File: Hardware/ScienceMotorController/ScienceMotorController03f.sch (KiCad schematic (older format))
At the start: 18 parts

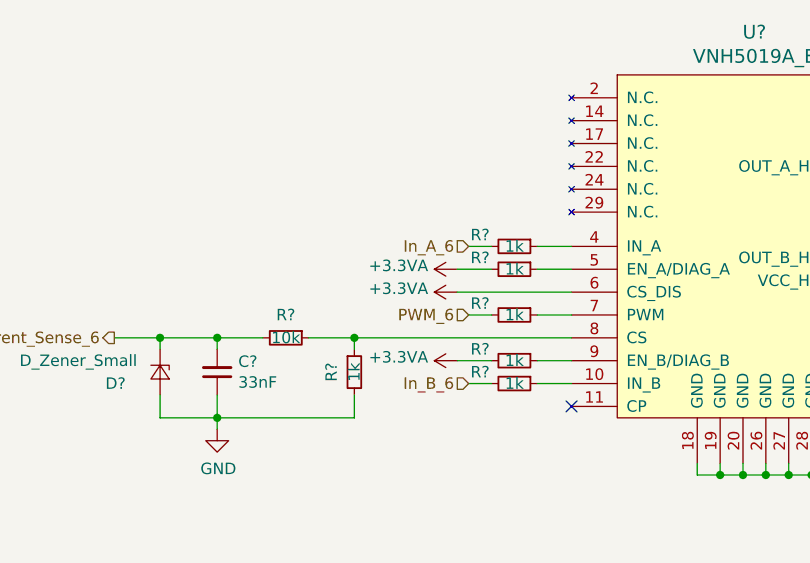
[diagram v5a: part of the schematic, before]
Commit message: Fixed 3.3V, added encoders
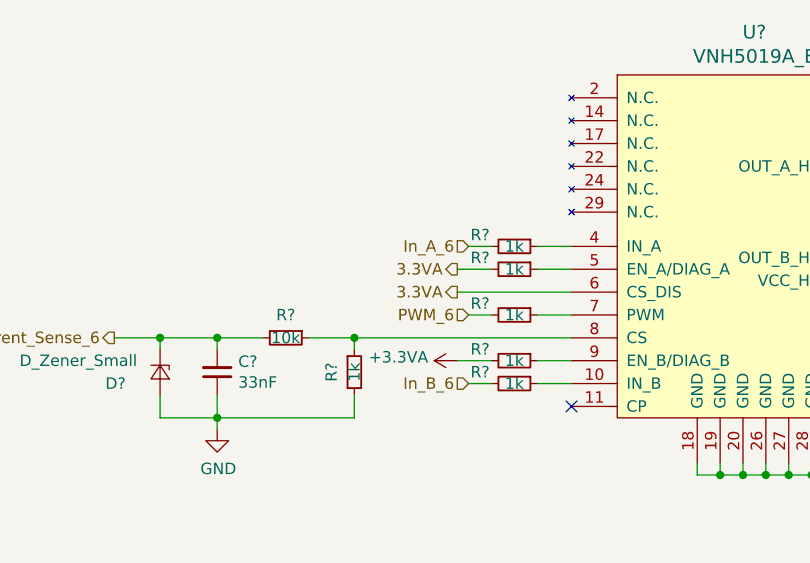
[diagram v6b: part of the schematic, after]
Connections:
- net +3.3VA: no longer R?.2, U?.6 (CS_DIS)
- new net 3.3VA: R?.2, U?.6 (CS_DIS)
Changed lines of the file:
@@
 $Descr A4 11693 8268
 encoding utf-8
-Sheet 8 10
+Sheet 8 11
 Title ""
 Date ""
@@
 $Comp
 L power:+3.3VA #PWR?
-U 1 1 5F83FF6A
-P 5150 3750
-AR Path="/5F7D111E/5FA66A7C/5F83FF6A" Ref="#PWR?"  Part="1"
-AR Path="/5F908300/5F83FF6A" Ref="#PWR?"  Part="1"
-AR Path="/5F7148FA/5FA34ADD/5F83FF6A" Ref="#PWR?"  Part="1"
-F 0 "#PWR?" H 5150 3600 50  0001 C CNN
-F 1 "+3.3VA" V 5165 3877 50  0000 L CNN
-F 2 "" H 5150 3750 50  0001 C CNN
-F 3 "" H 5150 3750 50  0001 C CNN
-	1    5150 3750
-	0    -1   -1   0
-$EndComp
-$Comp
-L power:+3.3VA #PWR?
-U 1 1 5F8408BA
-P 5150 3850
-AR Path="/5F7D111E/5FA66A7C/5F8408BA" Ref="#PWR?"  Part="1"
-AR Path="/5F908300/5F8408BA" Ref="#PWR?"  Part="1"
-AR Path="/5F7148FA/5FA34ADD/5F8408BA" Ref="#PWR?"  Part="1"
-F 0 "#PWR?" H 5150 3700 50  0001 C CNN
-F 1 "+3.3VA" V 5165 3977 50  0000 L CNN
-F 2 "" H 5150 3850 50  0001 C CNN
-F 3 "" H 5150 3850 50  0001 C CNN
-	1    5150 3850
-	0    -1   -1   0
-$EndComp
-$Comp
-L power:+3.3VA #PWR?
 U 1 1 5F840B1F
 P 5150 4150
@@
 Text HLabel 3650 4050 0    50   Output ~ 0
 Current_Sense_6
+Text HLabel 5150 3750 0    50   Output ~ 0
+3.3VA
+Text HLabel 5150 3850 0    50   Output ~ 0
+3.3VA
 $EndSCHEMATC

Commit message: added logic line
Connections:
- net 3.3VA is gone; now on net 3.3V: R?.2, U?.6 (CS_DIS)
- net +3.3VA renamed 3.3V
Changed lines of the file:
@@
-$EndComp
-$Comp
-L power:+3.3VA #PWR?
-U 1 1 5F840B1F
-P 5150 4150
-AR Path="/5F7D111E/5FA66A7C/5F840B1F" Ref="#PWR?"  Part="1"
-AR Path="/5F908300/5F840B1F" Ref="#PWR?"  Part="1"
-AR Path="/5F7148FA/5FA34ADD/5F840B1F" Ref="#PWR?"  Part="1"
-F 0 "#PWR?" H 5150 4000 50  0001 C CNN
-F 1 "+3.3VA" V 5165 4277 50  0000 L CNN
-F 2 "" H 5150 4150 50  0001 C CNN
-F 3 "" H 5150 4150 50  0001 C CNN
-	1    5150 4150
-	0    -1   -1   0
 $EndComp
 $Comp
@@
 Current_Sense_6
 Text HLabel 5150 3750 0    50   Output ~ 0
-3.3VA
+3.3V
 Text HLabel 5150 3850 0    50   Output ~ 0
-3.3VA
+3.3V
+Text HLabel 5150 4150 0    50   Output ~ 0
+3.3V
 $EndSCHEMATC

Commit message: annotated
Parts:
- C7: renamed from C?; footprint (none) -> Capacitor_SMD:C_0603_1608Metric_Pad1.05x0.95mm_HandSolder
- gave numbers to parts that had none: 16
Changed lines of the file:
@@
 AR Path="/5F7D111E/5FA66A7C/5FACB523" Ref="U?"  Part="1"
 AR Path="/5F908300/5FACB523" Ref="U?"  Part="1"
-AR Path="/5F7148FA/5FA34ADD/5FACB523" Ref="U?"  Part="1"
-F 0 "U?" H 6450 6087 60  0000 C CNN
+AR Path="/5F7148FA/5FA34ADD/5FACB523" Ref="U7"  Part="1"
+F 0 "U7" H 6450 6087 60  0000 C CNN
 F 1 "VNH5019A_E" H 6450 5981 60  0000 C CNN
 F 2 "" H 5850 5700 60  0001 C CNN
@@
 AR Path="/5F7D111E/5FA66A7C/5FACB540" Ref="R?"  Part="1"
 AR Path="/5F908300/5FACB540" Ref="R?"  Part="1"
-AR Path="/5F7148FA/5FA34ADD/5FACB540" Ref="R?"  Part="1"
-F 0 "R?" V 5350 3800 50  0000 C CNN
+AR Path="/5F7148FA/5FA34ADD/5FACB540" Ref="R46"  Part="1"
+F 0 "R46" V 5350 3800 50  0000 C CNN
 F 1 "1k" V 5400 3950 50  0000 C CNN
 F 2 "" H 5400 3950 50  0001 C CNN
@@
 AR Path="/5F7D111E/5FA66A7C/5FACB546" Ref="R?"  Part="1"
 AR Path="/5F908300/5FACB546" Ref="R?"  Part="1"
-AR Path="/5F7148FA/5FA34ADD/5FACB546" Ref="R?"  Part="1"
-F 0 "R?" V 4600 4200 50  0000 C CNN
+AR Path="/5F7148FA/5FA34ADD/5FACB546" Ref="R43"  Part="1"
+F 0 "R43" V 4600 4200 50  0000 C CNN
 F 1 "1k" V 4700 4200 50  0000 C CNN
 F 2 "" H 4700 4200 50  0001 C CNN
@@
 AR Path="/5F7D111E/5FA66A7C/5FACB54C" Ref="C?"  Part="1"
 AR Path="/5F908300/5FACB54C" Ref="C?"  Part="1"
-AR Path="/5F7148FA/5FA34ADD/5FACB54C" Ref="C?"  Part="1"
-F 0 "C?" H 4008 4154 50  0000 R CNN
+AR Path="/5F7148FA/5FA34ADD/5FACB54C" Ref="C7"  Part="1"
+F 0 "C7" H 4008 4154 50  0000 R CNN
 F 1 "33nF" H 4008 4245 50  0000 R CNN
-F 2 "" H 4100 4200 50  0001 C CNN
+F 2 "Capacitor_SMD:C_0603_1608Metric_Pad1.05x0.95mm_HandSolder" H 4100 4200 50  0001 C CNN
 F 3 "~" H 4100 4200 50  0001 C CNN
 	1    4100 4200
@@
 AR Path="/5F7D111E/5FA66A7C/5FACB552" Ref="D?"  Part="1"
 AR Path="/5F908300/5FACB552" Ref="D?"  Part="1"
-AR Path="/5F7148FA/5FA34ADD/5FACB552" Ref="D?"  Part="1"
-F 0 "D?" V 3900 4050 50  0000 R CNN
+AR Path="/5F7148FA/5FA34ADD/5FACB552" Ref="D19"  Part="1"
+F 0 "D19" V 3900 4050 50  0000 R CNN
 F 1 "D_Zener_Small" V 3800 4100 50  0000 R CNN
 F 2 "" V 3850 4200 50  0001 C CNN
@@
 AR Path="/5F7D111E/5FA66A7C/5FACB558" Ref="R?"  Part="1"
 AR Path="/5F908300/5FACB558" Ref="R?"  Part="1"
-AR Path="/5F7148FA/5FA34ADD/5FACB558" Ref="R?"  Part="1"
-F 0 "R?" V 4300 4050 50  0000 C CNN
+AR Path="/5F7148FA/5FA34ADD/5FACB558" Ref="R42"  Part="1"
+F 0 "R42" V 4300 4050 50  0000 C CNN
 F 1 "10k" V 4400 4050 50  0000 C CNN
 F 2 "" H 4400 4050 50  0001 C CNN
@@
 AR Path="/5F7D111E/5FA66A7C/5FACB56E" Ref="R?"  Part="1"
 AR Path="/5F908300/5FACB56E" Ref="R?"  Part="1"
-AR Path="/5F7148FA/5FA34ADD/5FACB56E" Ref="R?"  Part="1"
-F 0 "R?" V 5350 4000 50  0000 C CNN
+AR Path="/5F7148FA/5FA34ADD/5FACB56E" Ref="R47"  Part="1"
+F 0 "R47" V 5350 4000 50  0000 C CNN
 F 1 "1k" V 5400 4150 50  0000 C CNN
 F 2 "" H 5400 4150 50  0001 C CNN
@@
 AR Path="/5F7D111E/5FA66A7C/5FACB583" Ref="R?"  Part="1"
 AR Path="/5F908300/5FACB583" Ref="R?"  Part="1"
-AR Path="/5F7148FA/5FA34ADD/5FACB583" Ref="R?"  Part="1"
-F 0 "R?" V 5350 3600 50  0000 C CNN
+AR Path="/5F7148FA/5FA34ADD/5FACB583" Ref="R45"  Part="1"
+F 0 "R45" V 5350 3600 50  0000 C CNN
 F 1 "1k" V 5400 3750 50  0000 C CNN
 F 2 "" H 5400 3750 50  0001 C CNN
@@
 AR Path="/5F7D111E/5FA66A7C/5FACB591" Ref="R?"  Part="1"
 AR Path="/5F908300/5FACB591" Ref="R?"  Part="1"
-AR Path="/5F7148FA/5FA34ADD/5FACB591" Ref="R?"  Part="1"
-F 0 "R?" V 5350 3500 50  0000 C CNN
+AR Path="/5F7148FA/5FA34ADD/5FACB591" Ref="R44"  Part="1"
+F 0 "R44" V 5350 3500 50  0000 C CNN
 F 1 "1k" V 5400 3650 50  0000 C CNN
 F 2 "" H 5400 3650 50  0001 C CNN
@@
 AR Path="/5F7D111E/5FA66A7C/5FACB59B" Ref="R?"  Part="1"
 AR Path="/5F908300/5FACB59B" Ref="R?"  Part="1"
-AR Path="/5F7148FA/5FA34ADD/5FACB59B" Ref="R?"  Part="1"
-F 0 "R?" V 5350 4100 50  0000 C CNN
+AR Path="/5F7148FA/5FA34ADD/5FACB59B" Ref="R48"  Part="1"
+F 0 "R48" V 5350 4100 50  0000 C CNN
 F 1 "1k" V 5400 4250 50  0000 C CNN
 F 2 "" H 5400 4250 50  0001 C CNN
@@
 AR Path="/5F7D111E/5FA66A7C/5FACB5B3" Ref="#PWR?"  Part="1"
 AR Path="/5F908300/5FACB5B3" Ref="#PWR?"  Part="1"
-AR Path="/5F7148FA/5FA34ADD/5FACB5B3" Ref="#PWR?"  Part="1"
-F 0 "#PWR?" H 6800 4450 50  0001 C CNN
+AR Path="/5F7148FA/5FA34ADD/5FACB5B3" Ref="#PWR037"  Part="1"
+F 0 "#PWR037" H 6800 4450 50  0001 C CNN
 F 1 "GND" H 6805 4527 50  0000 C CNN
 F 2 "" H 6800 4700 50  0001 C CNN
@@
 AR Path="/5F7D111E/5FA66A7C/5FACB5BD" Ref="#PWR?"  Part="1"
 AR Path="/5F908300/5FACB5BD" Ref="#PWR?"  Part="1"
-AR Path="/5F7148FA/5FA34ADD/5FACB5BD" Ref="#PWR?"  Part="1"
-F 0 "#PWR?" H 4100 4200 50  0001 C CNN
+AR Path="/5F7148FA/5FA34ADD/5FACB5BD" Ref="#PWR036"  Part="1"
+F 0 "#PWR036" H 4100 4200 50  0001 C CNN
 F 1 "GND" H 4105 4277 50  0000 C CNN
 F 2 "" H 4100 4450 50  0001 C CNN
@@
 AR Path="/5F7D111E/5FA66A7C/5FACB5D5" Ref="Conn?"  Part="1"
 AR Path="/5F908300/5FACB5D5" Ref="Conn?"  Part="1"
-AR Path="/5F7148FA/5FA34ADD/5FACB5D5" Ref="Conn?"  Part="1"
-F 0 "Conn?" H 8522 3347 60  0000 R CNN
+AR Path="/5F7148FA/5FA34ADD/5FACB5D5" Ref="Conn6"  Part="1"
+F 0 "Conn6" H 8522 3347 60  0000 R CNN
 F 1 "AndersonPP" H 8522 3453 60  0000 R CNN
 F 2 "" H 8400 2750 60  0001 C CNN
@@
 AR Path="/5F7D111E/5FA66A7C/5FACB5DB" Ref="Conn?"  Part="2"
 AR Path="/5F908300/5FACB5DB" Ref="Conn?"  Part="2"
-AR Path="/5F7148FA/5FA34ADD/5FACB5DB" Ref="Conn?"  Part="2"
-F 0 "Conn?" H 8522 2947 60  0000 R CNN
+AR Path="/5F7148FA/5FA34ADD/5FACB5DB" Ref="Conn6"  Part="2"
+F 0 "Conn6" H 8522 2947 60  0000 R CNN
 F 1 "AndersonPP" H 8522 3053 60  0000 R CNN
 F 2 "" H 8400 2350 60  0001 C CNN
@@
 AR Path="/5F7D111E/5FA66A7C/5FACB5EF" Ref="D?"  Part="1"
 AR Path="/5F908300/5FACB5EF" Ref="D?"  Part="1"
-AR Path="/5F7148FA/5FA34ADD/5FACB5EF" Ref="D?"  Part="1"
-F 0 "D?" H 8400 3150 50  0000 C CNN
+AR Path="/5F7148FA/5FA34ADD/5FACB5EF" Ref="D20"  Part="1"
+F 0 "D20" H 8400 3150 50  0000 C CNN
 F 1 "Blue_LED" H 8450 3250 31  0000 C CNN
 F 2 "" V 8300 3200 50  0001 C CNN
@@
 AR Path="/5F7D111E/5FA66A7C/5FACB5F5" Ref="D?"  Part="1"
 AR Path="/5F908300/5FACB5F5" Ref="D?"  Part="1"
-AR Path="/5F7148FA/5FA34ADD/5FACB5F5" Ref="D?"  Part="1"
-F 0 "D?" H 8400 3550 50  0000 C CNN
+AR Path="/5F7148FA/5FA34ADD/5FACB5F5" Ref="D21"  Part="1"
+F 0 "D21" H 8400 3550 50  0000 C CNN
 F 1 "Blue_LED" H 8450 3650 31  0000 C CNN
 F 2 "" V 8300 3600 50  0001 C CNN
@@
 AR Path="/5F7D111E/5FA66A7C/5FACB5FB" Ref="R?"  Part="1"
 AR Path="/5F908300/5FACB5FB" Ref="R?"  Part="1"
-AR Path="/5F7148FA/5FA34ADD/5FACB5FB" Ref="R?"  Part="1"
-F 0 "R?" V 8500 3500 50  0000 C CNN
+AR Path="/5F7148FA/5FA34ADD/5FACB5FB" Ref="R50"  Part="1"
+F 0 "R50" V 8500 3500 50  0000 C CNN
 F 1 "1.5k" V 8550 3600 39  0000 C CNN
 F 2 "" H 8550 3600 50  0001 C CNN
@@
 AR Path="/5F7D111E/5FA66A7C/5FACB601" Ref="R?"  Part="1"
 AR Path="/5F908300/5FACB601" Ref="R?"  Part="1"
-AR Path="/5F7148FA/5FA34ADD/5FACB601" Ref="R?"  Part="1"
-F 0 "R?" V 8500 3100 50  0000 C CNN
+AR Path="/5F7148FA/5FA34ADD/5FACB601" Ref="R49"  Part="1"
+F 0 "R49" V 8500 3100 50  0000 C CNN
 F 1 "1.5k" V 8550 3200 39  0000 C CNN
 F 2 "" H 8550 3200 50  0001 C CNN
@@
 AR Path="/5F7D111E/5FA66A7C/5FACB609" Ref="#PWR?"  Part="1"
 AR Path="/5F908300/5FACB609" Ref="#PWR?"  Part="1"
-AR Path="/5F7148FA/5FA34ADD/5FACB609" Ref="#PWR?"  Part="1"
-F 0 "#PWR?" H 8750 2950 50  0001 C CNN
+AR Path="/5F7148FA/5FA34ADD/5FACB609" Ref="#PWR039"  Part="1"
+F 0 "#PWR039" H 8750 2950 50  0001 C CNN
 F 1 "GND" V 8755 3072 50  0000 R CNN
 F 2 "" H 8750 3200 50  0001 C CNN
@@
 AR Path="/5F7D111E/5FA66A7C/5FACB60F" Ref="#PWR?"  Part="1"
 AR Path="/5F908300/5FACB60F" Ref="#PWR?"  Part="1"
-AR Path="/5F7148FA/5FA34ADD/5FACB60F" Ref="#PWR?"  Part="1"
-F 0 "#PWR?" H 8750 3350 50  0001 C CNN
+AR Path="/5F7148FA/5FA34ADD/5FACB60F" Ref="#PWR040"  Part="1"
+F 0 "#PWR040" H 8750 3350 50  0001 C CNN
 F 1 "GND" V 8755 3472 50  0000 R CNN
 F 2 "" H 8750 3600 50  0001 C CNN
@@
 AR Path="/5F7D111E/5FA66A7C/5F83E921" Ref="FB?"  Part="1"
 AR Path="/5F908300/5F83E921" Ref="FB?"  Part="1"
-AR Path="/5F7148FA/5FA34ADD/5F83E921" Ref="FB?"  Part="1"
-F 0 "FB?" V 7850 3400 50  0000 L CNN
+AR Path="/5F7148FA/5FA34ADD/5F83E921" Ref="FB10"  Part="1"
+F 0 "FB10" V 7850 3400 50  0000 L CNN
 F 1 "Frte_Bd" V 7650 3250 50  0000 L CNN
 F 2 "" V 7680 3400 50  0001 C CNN
@@
 AR Path="/5F7D111E/5FA66A7C/5F8410BA" Ref="#PWR?"  Part="1"
 AR Path="/5F908300/5F8410BA" Ref="#PWR?"  Part="1"
-AR Path="/5F7148FA/5FA34ADD/5F8410BA" Ref="#PWR?"  Part="1"
-F 0 "#PWR?" H 7500 3800 50  0001 C CNN
+AR Path="/5F7148FA/5FA34ADD/5F8410BA" Ref="#PWR038"  Part="1"
+F 0 "#PWR038" H 7500 3800 50  0001 C CNN
 F 1 "+12VA" H 7515 4123 50  0000 C CNN
 F 2 "" H 7500 3950 50  0001 C CNN
@@
 AR Path="/5F7D111E/5FA66A7C/5F82955C" Ref="FB?"  Part="1"
 AR Path="/5F908300/5F82955C" Ref="FB?"  Part="1"
-AR Path="/5F7148FA/5FA34ADD/5F82955C" Ref="FB?"  Part="1"
-F 0 "FB?" V 7950 3050 50  0000 L CNN
+AR Path="/5F7148FA/5FA34ADD/5F82955C" Ref="FB9"  Part="1"
+F 0 "FB9" V 7950 3050 50  0000 L CNN
 F 1 "Frte_Bd" V 7850 2900 50  0000 L CNN
 F 2 "" V 7680 3000 50  0001 C CNN
